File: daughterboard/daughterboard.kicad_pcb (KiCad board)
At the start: 2 copper layers, 85 x 56 mm, 38 parts, among them CON1 12V_JACK, IC1 ATMEGA328P-A, P1 EXTRA_PB01, P2 EXTRA_PC12345, P3 CONN_13X2, P4 AZIMUTH, P5 ELEVATION, P6 EXTRA_ADC67, P7 VALVE, Q1 TIP120, U1 ULN2803A, Y1 8MHz

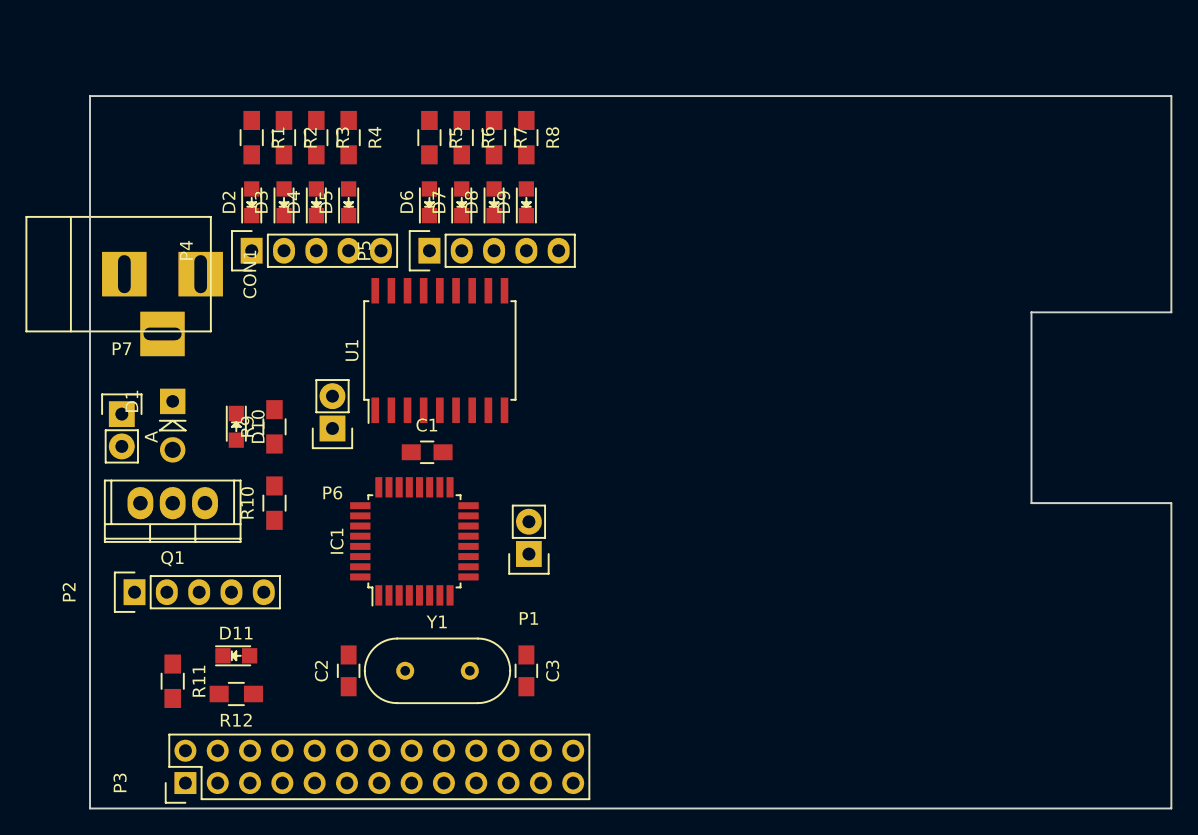
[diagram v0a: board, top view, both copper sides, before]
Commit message: fix board size to allow use of camera port, add keepouts for mounting holes
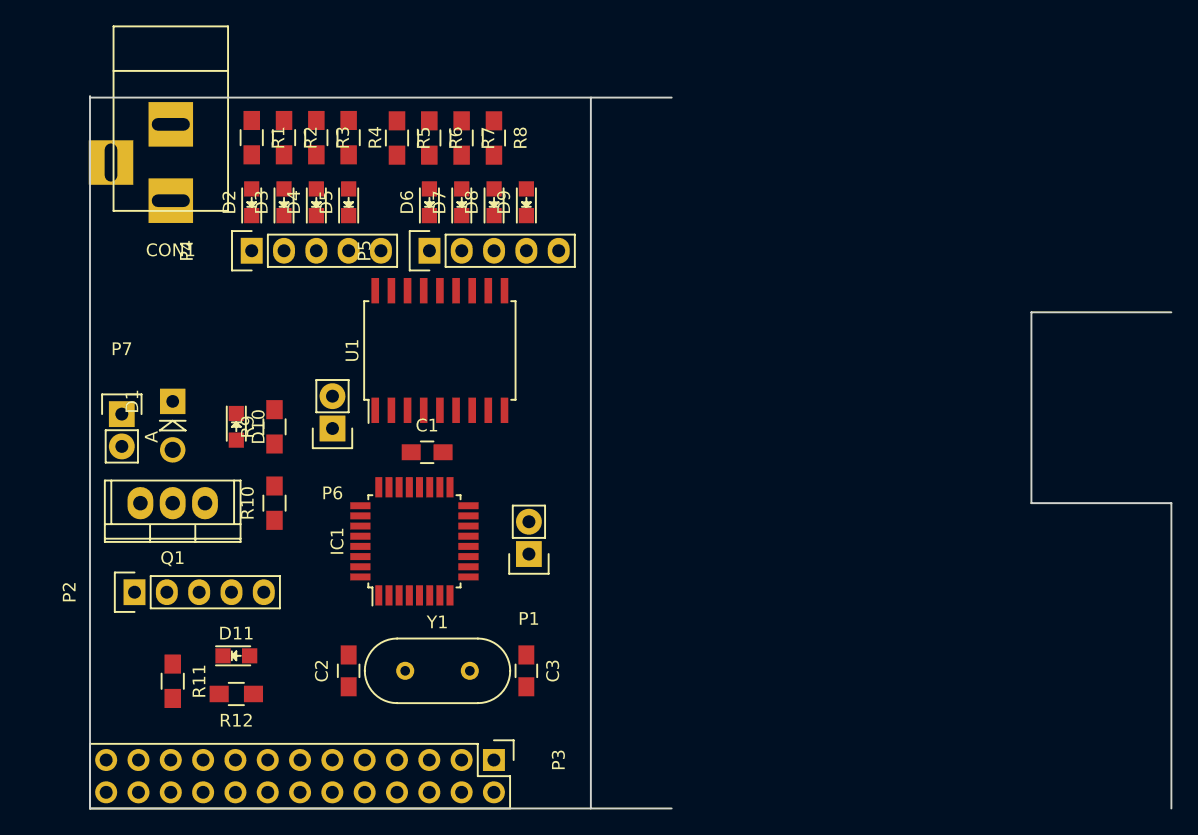
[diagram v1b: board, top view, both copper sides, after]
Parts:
- moved P3 24.3 mm to (175.2, 177.2), turned to 270 degrees
- moved CON1 12.6 mm to (149.8, 127.0), turned to 270 degrees
- moved R5 2.55 mm to (167.6, 128.3)
- moved R6 2.55 mm to (170.2, 128.3)
- moved R8 2.55 mm to (175.2, 128.3)
- moved R7 2.55 mm to (172.7, 128.3)
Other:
- outline, holes or cut-outs redrawn

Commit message: Reassign pins around to simplify layout
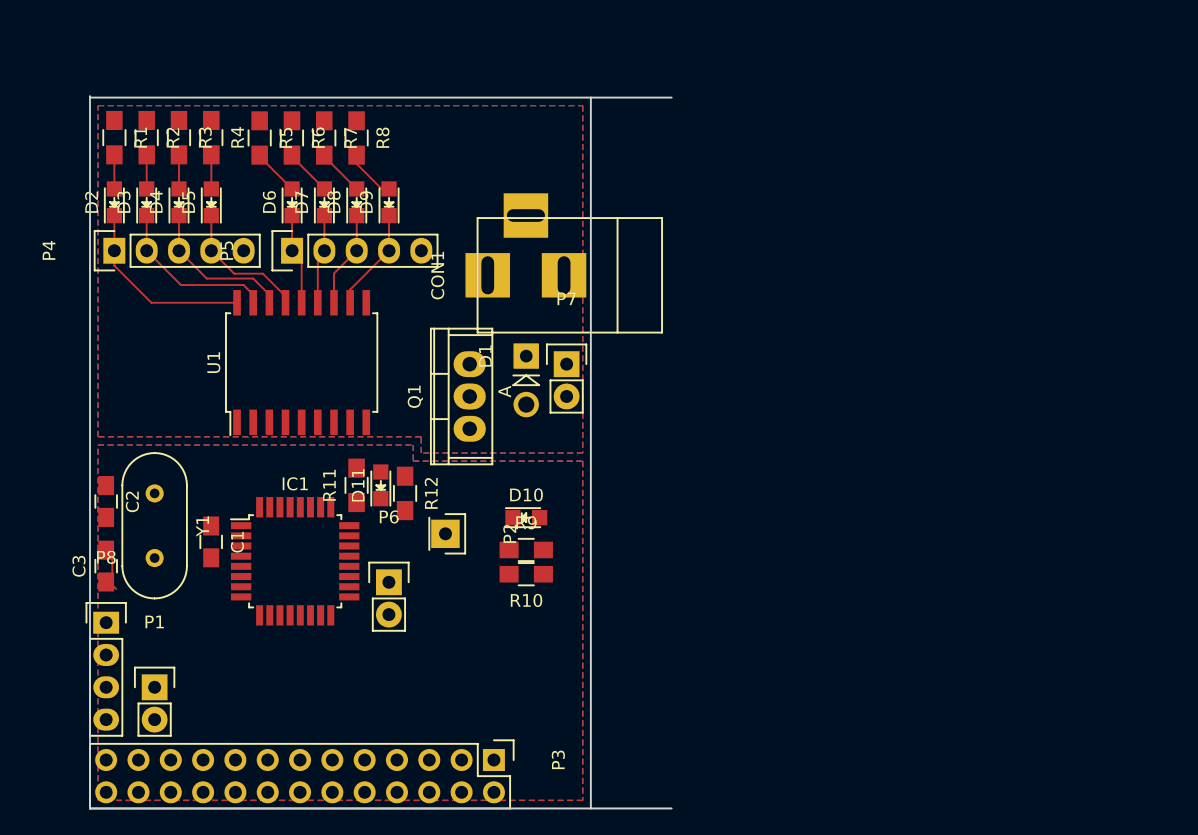
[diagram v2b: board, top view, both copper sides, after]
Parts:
- added P8: X_PD4567, Pin_Headers:Pin_Header_Straight_1x04, F.Cu at (144.8, 166.4)
- P1: value EXTRA_PB01 -> X_PB01
- P2: value EXTRA_PC12345 -> X_PC1; footprint Pin_Headers:Pin_Header_Straight_1x05 -> Pin_Headers:Pin_Header_Straight_1x01
- P6: value EXTRA_ADC67 -> X_ADC67
- moved P7 35.2 mm to (181.0, 146.1)
- moved C3 34.0 mm to (144.8, 161.9), turned to 90 degrees
- moved CON1 33.4 mm to (181.0, 139.1), turned to 180 degrees
- moved P1 31.2 mm to (148.6, 171.5), turned to 0 degrees
- moved D1 28.0 mm to (177.8, 145.4)
- moved Y1 25.0 mm to (148.6, 158.8), turned to 270 degrees
- moved P2 24.9 mm to (171.4, 159.4), turned to 270 degrees
- moved Q1 24.8 mm to (173.3, 148.6), turned to 90 degrees
- moved D10 23.9 mm to (177.8, 158.1), turned to 0 degrees
- moved C2 23.2 mm to (144.8, 156.9), turned to 270 degrees
- moved R9 22.0 mm to (177.8, 160.7), turned to 0 degrees
- moved R11 21.1 mm to (164.5, 155.6), turned to 90 degrees
- moved R12 20.6 mm to (168.3, 156.2), turned to 270 degrees
- moved R10 20.6 mm to (177.8, 162.6), turned to 180 degrees
- moved C1 18.4 mm to (153.0, 160.0), turned to 270 degrees
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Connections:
- D11 pad 1: /GPIO25 -> /GPIO4
- IC1 pad 1: Net-(IC1-Pad1) -> /S1
- IC1 pad 25: Net-(IC1-Pad25) -> /S8
- IC1 pad 26: Net-(IC1-Pad26) -> /S7
- IC1 pad 27: Net-(IC1-Pad27) -> /S6
- IC1 pad 28: Net-(IC1-Pad28) -> /S5
- IC1 pad 29: /GPIO25 -> /GPIO4
- IC1 pad 30: Net-(IC1-Pad30) -> /S4
- IC1 pad 31: Net-(IC1-Pad31) -> /S3
- IC1 pad 32: Net-(IC1-Pad32) -> /S2
- P3 pad 22: /GPIO25 -> (no net)
- P3 pad 7: (no net) -> /GPIO4
- R11 pad 1: /GPIO25 -> /GPIO4
- U1 pad 1: Net-(IC1-Pad30) -> /S1
- U1 pad 2: Net-(IC1-Pad31) -> /S2
- U1 pad 3: Net-(IC1-Pad32) -> /S3
- U1 pad 4: Net-(IC1-Pad1) -> /S4
- U1 pad 5: Net-(IC1-Pad2) -> /S5
- U1 pad 6: Net-(IC1-Pad9) -> /S6
- U1 pad 7: Net-(IC1-Pad10) -> /S7
- U1 pad 8: Net-(IC1-Pad11) -> /S8
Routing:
- net Net-(D2-Pad1): track 0.00 -> 14.8 mm
- net Net-(D3-Pad1): track 0.00 -> 13.2 mm
- net Net-(D4-Pad1): track 0.00 -> 11.9 mm
- net Net-(D5-Pad1): track 0.00 -> 10.6 mm
- net Net-(D9-Pad1): track 0.00 -> 8.12 mm
- net Net-(D8-Pad1): track 0.00 -> 7.59 mm
- net Net-(D6-Pad1): track 0.00 -> 7.16 mm
- net Net-(D7-Pad1): track 0.00 -> 7.06 mm
- net Net-(D9-Pad2): track 0.00 -> 4.05 mm
- net Net-(D8-Pad2): track 0.00 -> 3.71 mm
- net Net-(D7-Pad2): track 0.00 -> 3.71 mm
- net Net-(D6-Pad2): track 0.00 -> 3.71 mm
- net /XTAL2: track 0.00 -> 2.70 mm
- net Net-(D5-Pad2): track 0.00 -> 2.68 mm
- net Net-(D4-Pad2): track 0.00 -> 2.68 mm
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- added copper zone on B.Cu, net +12V
- added copper zone on B.Cu, net +3V3
- added copper zone on F.Cu, net GND
- added copper zone on F.Cu, net GNDD
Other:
- board size 85 x 56 mm -> 45.7 x 56 mm
- net class Default: clearance 0.2 -> 0.1524; trace_width 0.2 -> 0.1524; via_dia 0.9 -> 0.6858; via_drill 0.6 -> 0.3302
- net class Power: clearance 0.2 -> 0.508; trace_width 0.5 -> 0.508; via_dia 1 -> 0.6858; via_drill 0.7 -> 0.3302
- rule trace_clearance: 0.2 -> 0.1524
- rule via_min_drill: 0.5 -> 0.3302
- rule via_min_size: 0.8 -> 0.6858

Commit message: Route everything except optional headers
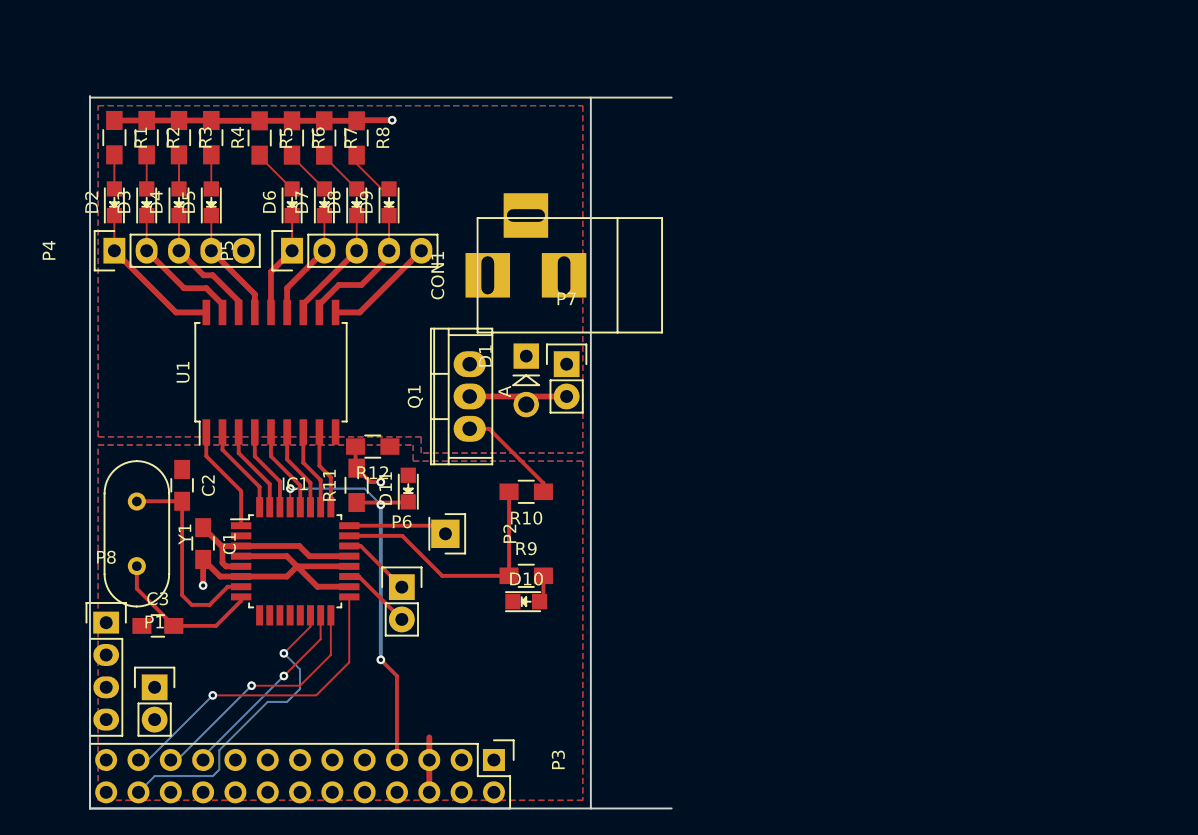
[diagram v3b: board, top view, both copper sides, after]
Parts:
- D10: value YELLOW -> VALVE
- D11: value RED -> RESET
- moved D10 6.60 mm to (177.8, 164.7)
- moved R10 6.48 mm to (177.8, 156.1)
- moved C3 6.21 mm to (148.8, 166.6), turned to 0 degrees
- moved C2 6.10 mm to (150.7, 155.6)
- moved R12 4.47 mm to (165.7, 152.6), turned to 180 degrees
- moved U1 2.53 mm to (157.7, 146.7)
- moved D11 2.17 mm to (168.5, 155.9)
- moved R9 2.03 mm to (177.8, 162.7)
- moved Y1 1.53 mm to (147.2, 159.4)
- moved P6 1.09 mm to (168.0, 163.6)
- moved C1 0.65 mm to (152.4, 160.2)
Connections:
- P3 pad 5: (no net) -> GNDD
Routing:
- net /GPIO4: track 0.00 -> 34.0 mm, vias 0 -> 3
- net +12V: track 0.00 -> 30.7 mm, vias 0 -> 1
- net +3V3: track 0.00 -> 28.0 mm, vias 0 -> 2
- net /GPIO11(SCLK): track 0.00 -> 24.9 mm, vias 0 -> 1
- net /GPIO8(CE0): track 0.00 -> 24.8 mm, vias 0 -> 1
- net /VALVE: track 0.00 -> 20.5 mm
- net GNDD: track 0.43 -> 20.0 mm
- net /GPIO9(MISO): track 0.00 -> 19.1 mm, vias 0 -> 1
- net /XTAL1: track 0.00 -> 16.5 mm
- net /GPIO10(MOSI): track 0.00 -> 15.2 mm, vias 0 -> 1
- net /XTAL2: track 2.70 -> 12.3 mm
- net Net-(IC1-Pad24): track 0.00 -> 8.73 mm
- net /S1: track 0.00 -> 8.49 mm
- net Net-(Q1-Pad1): track 0.00 -> 8.25 mm
- net Net-(D1-Pad2): track 0.00 -> 7.62 mm
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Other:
- net class Power: clearance 0.508 -> 0.3048; trace_width 0.508 -> 0.3048
